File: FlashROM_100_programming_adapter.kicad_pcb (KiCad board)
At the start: 2 copper layers, 16.8 x 34.5 mm, 3 parts, among them J1 LH535618 Socket, U1 28C256 pinout to programmer

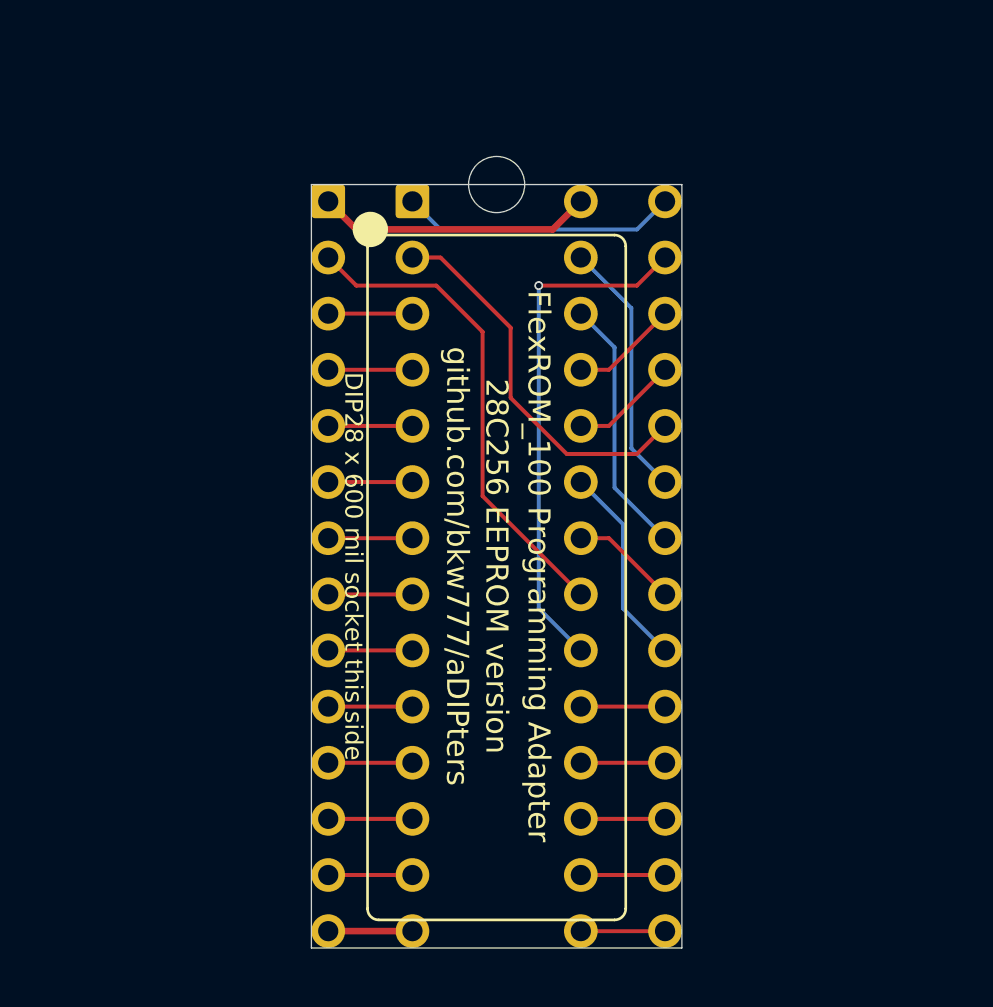
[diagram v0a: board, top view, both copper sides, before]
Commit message: Add FlashROM_100. /WE pin on FlexROM_100
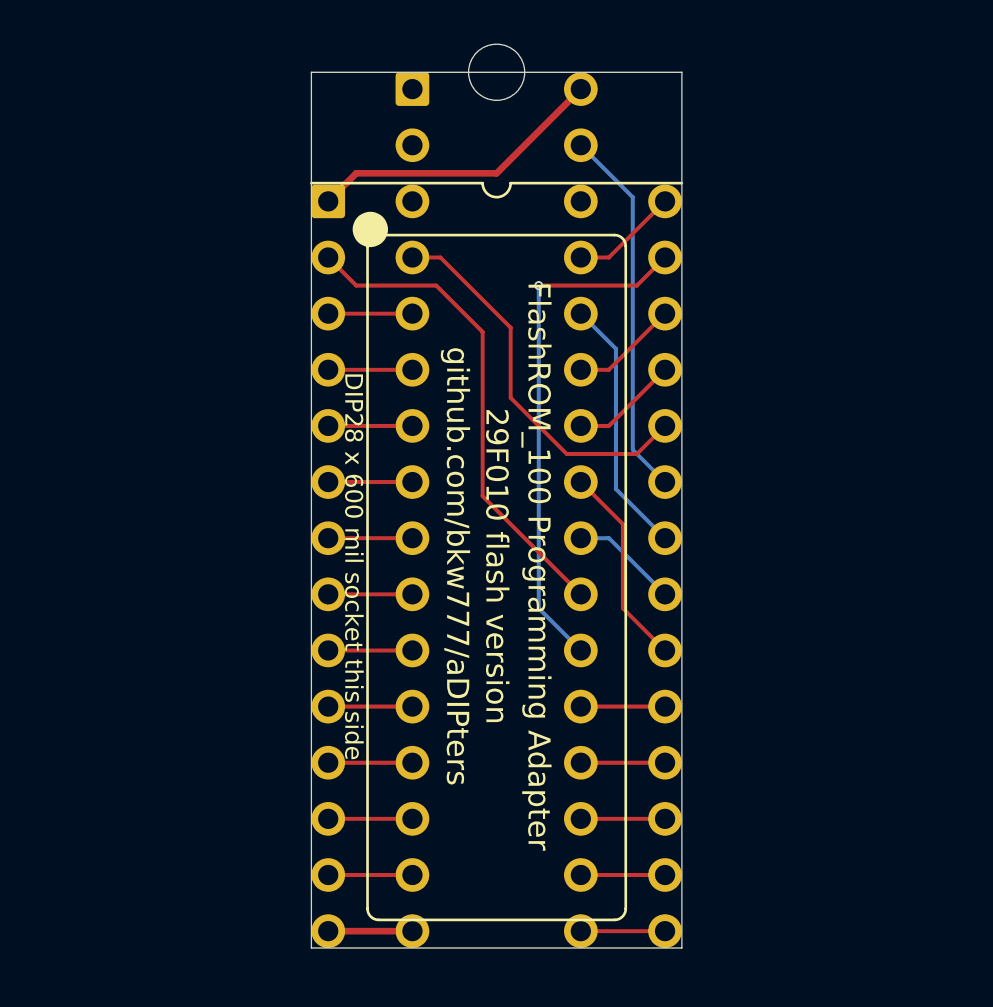
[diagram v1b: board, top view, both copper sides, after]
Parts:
- U1: value 28C256 pinout to programmer -> 29F010 pins to programmer; footprint 000_LOCAL:2x28_0.3_0.1_pins -> 000_LOCAL:DIP32_0.3
- moved polarity notch 5.08 mm to (150.0, 77.6)
- moved U1 2.54 mm to (150.0, 97.5)
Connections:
- U1 pad 1: /A14 -> (no net)
- U1 pad 10: /A0 -> /A2
- U1 pad 11: /D0 -> /A1
- U1 pad 12: /D1 -> /A0
- U1 pad 13: /D2 -> /D0
- U1 pad 14: /GND -> /D1
- U1 pad 15: /D3 -> /D2
- U1 pad 16: /D4 -> /GND
- U1 pad 17: /D5 -> /D3
- U1 pad 18: /D6 -> /D4
- U1 pad 19: /D7 -> /D5
- U1 pad 2: /A12 -> (no net)
- U1 pad 20: /~CE -> /D6
- U1 pad 21: /A10 -> /D7
- U1 pad 22: /~OE -> /~CE
- U1 pad 23: /A11 -> /A10
- U1 pad 24: /A9 -> /~OE
- U1 pad 25: /A8 -> /A11
- U1 pad 26: /A13 -> /A9
- U1 pad 27: /~WE -> /A8
- U1 pad 28: /VCC -> /A13
- U1 pad 3: /A7 -> (no net)
- U1 pad 4: /A6 -> /A12
- U1 pad 5: /A5 -> /A7
- U1 pad 6: /A4 -> /A6
- U1 pad 7: /A3 -> /A5
- U1 pad 8: /A2 -> /A4
- U1 pad 9: /A1 -> /A3
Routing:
- net /A14: track 12.5 -> 4.86 mm
- net /~WE: track 11.7 -> 16.8 mm
- net /VCC: track 12.5 -> 13.5 mm
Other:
- board size 16.8 x 34.5 mm -> 16.8 x 39.6 mm
- board text added: "29F010 flash version"
- board text added: "FlashROM_100 Programming Adapter"
- board text removed: "28C256 EEPROM version"
- board text removed: "FlexROM_100 Programming Adapter"
- board text removed: "tandy.wiki/FlexROM_100"

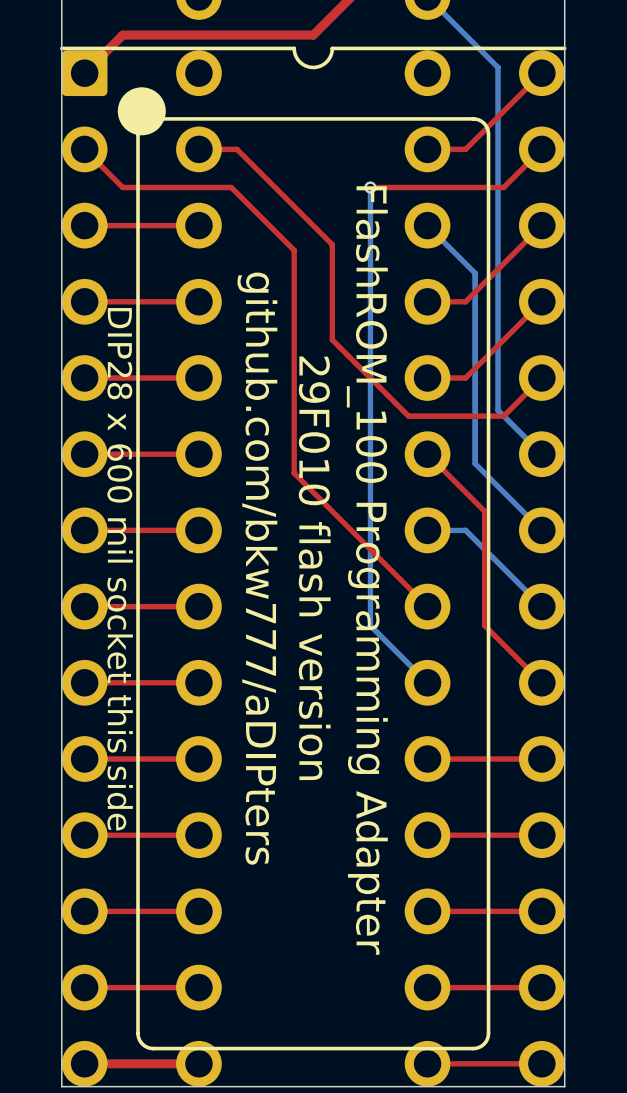
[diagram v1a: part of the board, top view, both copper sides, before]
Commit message: add FlashROM_100_tsop
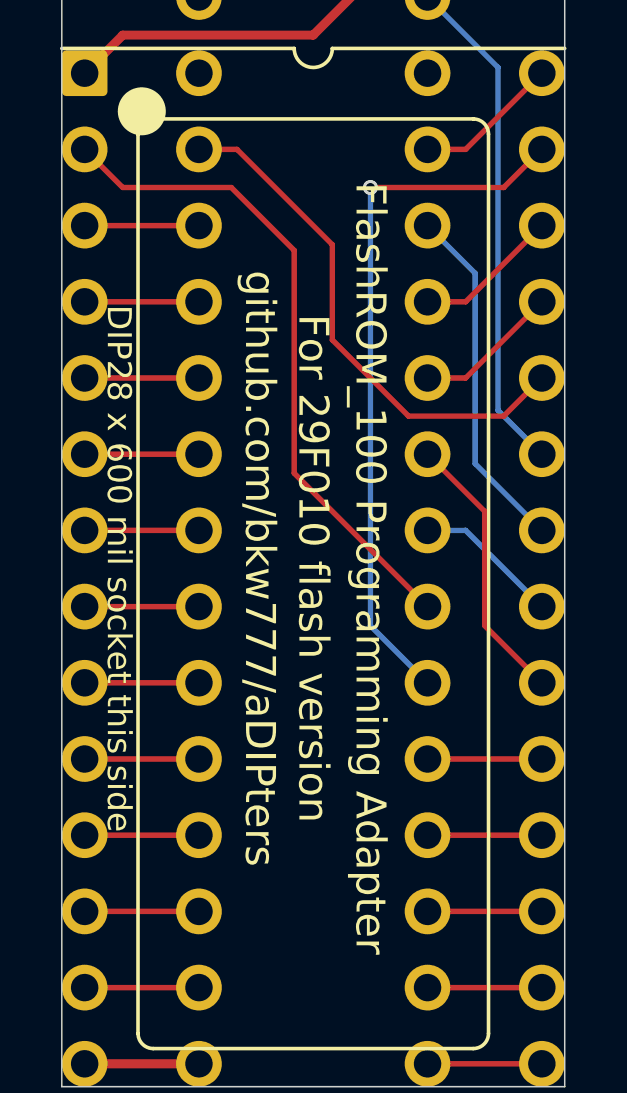
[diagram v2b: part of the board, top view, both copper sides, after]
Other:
- net class Default: via_dia 0.4 -> 0.5; via_drill 0.25 -> 0.3
- rule via_min_drill: 0.25 -> 0.3
- rule via_min_size: 0.4 -> 0.5
- board text added: "For 29F010 flash version"
- board text removed: "29F010 flash version"
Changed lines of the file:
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@@
-(kicad_pcb (version 20171130) (host pcbnew 5.1.7-a382d34a8~87~ubuntu20.04.1)
+(kicad_pcb (version 20171130) (host pcbnew 5.1.9-73d0e3b20d~88~ubuntu20.10.1)
   (general
     (thickness 1.6)
@@
     (nets 29)
   )
-  (page A4)
+  (page USLetter)
+  (title_block
+    (title "Programming Adapter for FlashROM_100")
+    (date 2021-03-07)
+    (rev 002)
+    (company "Brian K. White - b.kenyon.w@gmail.com")
+  )
   (layers
     (0 F.Cu signal)
@@
     (zone_45_only no)
     (trace_min 0.16)
-    (via_size 0.4)
-    (via_drill 0.25)
-    (via_min_size 0.4)
-    (via_min_drill 0.25)
-    (uvia_size 0.4)
-    (uvia_drill 0.25)
+    (via_size 0.5)
+    (via_drill 0.3)
+    (via_min_size 0.5)
+    (via_min_drill 0.3)
+    (uvia_size 0.5)
+    (uvia_drill 0.3)
     (uvias_allowed no)
-    (uvia_min_size 0.4)
-    (uvia_min_drill 0.25)
+    (uvia_min_size 0.5)
+    (uvia_min_drill 0.3)
     (edge_width 0.05)
     (segment_width 0.2)
@@
     (pad_drill 0.9144)
     (pad_to_mask_clearance 0)
+    (solder_mask_min_width 0.22)
     (aux_axis_origin 0 0)
     (grid_origin 150 100)
@@
       (outputformat 1)
       (mirror false)
-      (drillshape 1)
+      (drillshape 0)
       (scaleselection 1)
-      (outputdirectory ""))
+      (outputdirectory "GERBER_FlashROM_100_programming_adapter"))
   )
   (net 0 "")
@@
     (clearance 0.16)
     (trace_width 0.18)
-    (via_dia 0.4)
-    (via_drill 0.25)
-    (uvia_dia 0.4)
-    (uvia_drill 0.25)
+    (via_dia 0.5)
+    (via_drill 0.3)
+    (uvia_dia 0.5)
+    (uvia_drill 0.3)
     (add_net /A0)
     (add_net /A1)
@@
       (effects (font (size 1 1) (thickness 0.15)))
     )
+    (fp_line (start -8.382 -17.272) (end -8.382 17.272) (layer F.CrtYd) (width 0.01))
+    (fp_line (start -8.382 17.272) (end 8.382 17.272) (layer F.CrtYd) (width 0.01))
+    (fp_line (start 8.382 17.272) (end 8.382 -17.272) (layer F.CrtYd) (width 0.01))
     (fp_line (start 8.382 -17.272) (end -8.382 -17.272) (layer F.CrtYd) (width 0.01))
-    (fp_line (start 8.382 17.272) (end 8.382 -17.272) (layer F.CrtYd) (width 0.01))
-    (fp_line (start -8.382 17.272) (end 8.382 17.272) (layer F.CrtYd) (width 0.01))
-    (fp_line (start -8.382 -17.272) (end -8.382 17.272) (layer F.CrtYd) (width 0.01))
     (fp_text user %R (at 0.27 3.12) (layer F.Fab)
       (effects (font (size 1 1) (thickness 0.15)))
@@
   (gr_arc (start 150 82.6645) (end 149.365 82.6645) (angle -180) (layer F.SilkS) (width 0.12))
   (gr_line (start 141.618 82.6645) (end 149.365 82.6645) (layer F.SilkS) (width 0.12))
-  (gr_text "29F010 flash version" (at 150 100 -90) (layer F.SilkS)
+  (gr_text "For 29F010 flash version" (at 150 100 -90) (layer F.SilkS)
     (effects (font (size 1 1) (thickness 0.15)))
   )
@@
   (segment (start 157.62 96.19) (end 156.1595 94.7295) (width 0.18) (layer B.Cu) (net 27))
   (segment (start 151.905 87.3) (end 151.905 87.3) (width 0.18) (layer F.Cu) (net 28))
-  (via (at 151.905 87.3) (size 0.4) (drill 0.25) (layers F.Cu B.Cu) (net 28))
+  (via (at 151.905 87.3) (size 0.5) (drill 0.3) (layers F.Cu B.Cu) (net 28) (status 1000000))
   (segment (start 151.905 101.905) (end 153.81 103.81) (width 0.18) (layer B.Cu) (net 28))
   (segment (start 151.905 87.3) (end 151.905 101.905) (width 0.18) (layer B.Cu) (net 28))

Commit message: kicad 6
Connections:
- net /~CE renamed /~{CE}
- net /~OE renamed /~{OE}
- net /~WE renamed /~{WE}
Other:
- net class Default removed

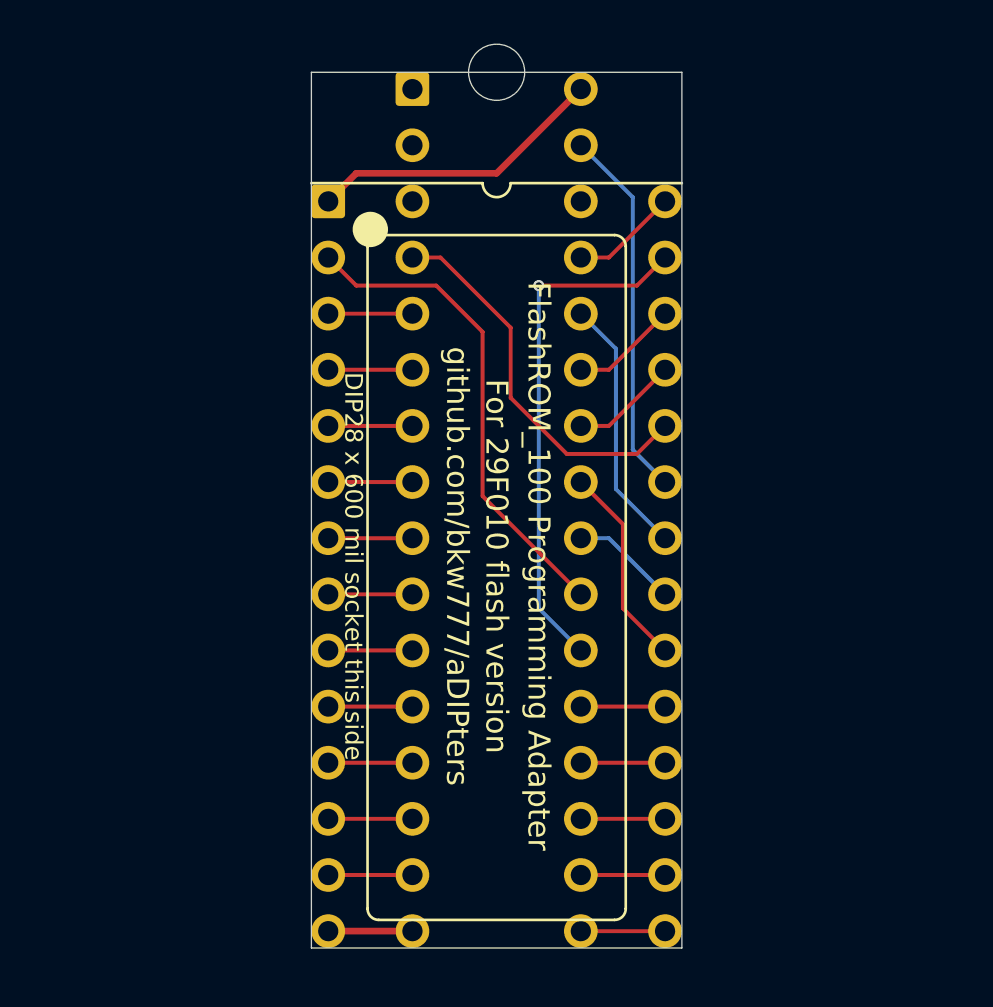
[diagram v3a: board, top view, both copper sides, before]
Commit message: Fix wrong pinout on FlashROM_100 TSOPgit add -A!
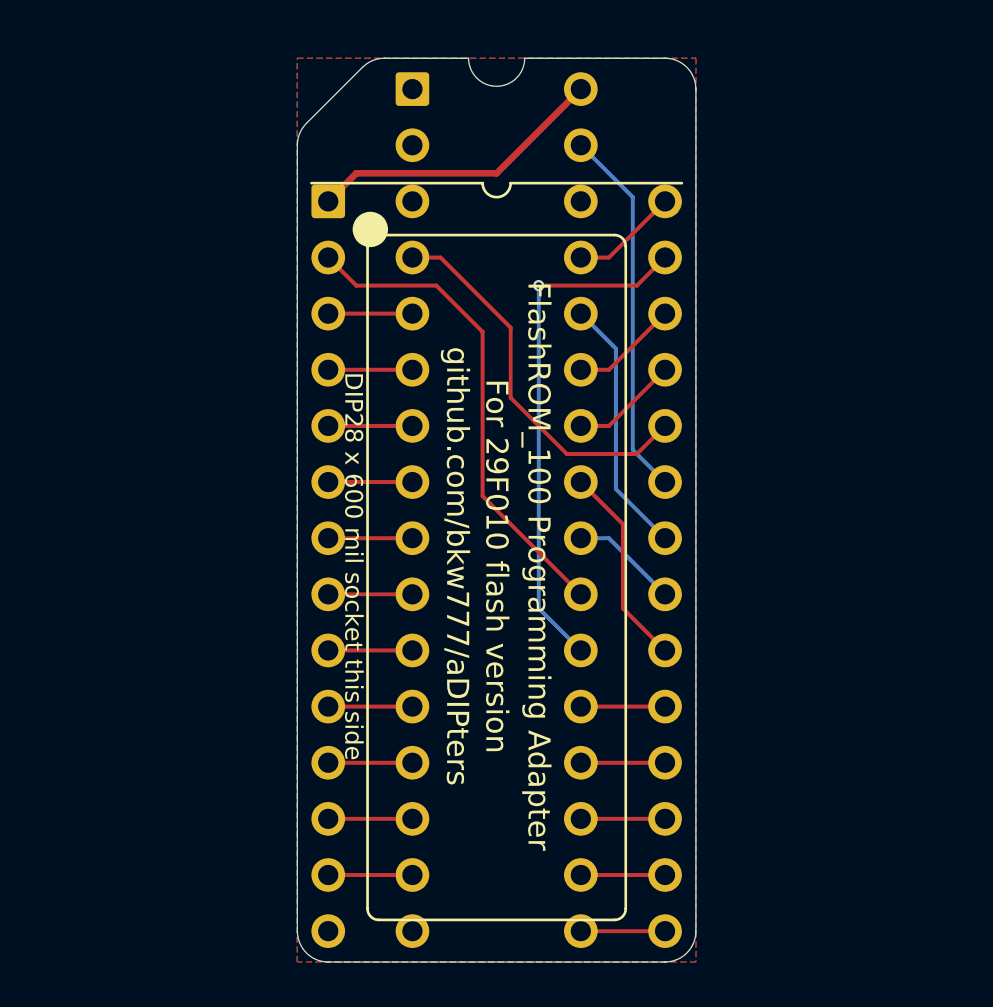
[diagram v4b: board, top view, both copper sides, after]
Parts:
- removed polarity notch: NPTH_0.1, 000_LOCAL:NPTH_0.1
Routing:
- net /GND: track 3.81 -> 0.00 mm
- added copper zone on B.Cu, net /GND
- added copper zone on F.Cu, net /GND
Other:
- board size 16.8 x 39.6 mm -> 18 x 40.9 mm
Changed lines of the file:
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@@
   (title_block
     (title "Programming Adapter for FlashROM_100")
-    (date "2021-03-07")
-    (rev "002")
+    (date "2022-10-11")
+    (rev "003")
     (company "Brian K. White - b.kenyon.w@gmail.com")
   )
@@
     )
   )
-  (footprint "000_LOCAL:NPTH_0.1" (layer "F.Cu")
-    (at 150 77.648)
-    (attr through_hole)
-    (fp_text reference "polarity notch" (at 0 2.54) (layer "F.SilkS") hide
-      (effects (font (size 1.27 1.27) (thickness 0.127)))
-    )
-    (fp_text value "NPTH_0.1" (at 0 -2.54) (layer "F.Fab")
-      (effects (font (size 1.27 1.27) (thickness 0.0127)))
-    )
-    (pad "" np_thru_hole circle locked (at 0 0) (size 2.54 2.54) (drill 2.54) (layers *.Cu *.Mask))
-  )
   (gr_line (start 152.54 77.7115) (end 155.08 77.7115) (layer "B.SilkS") (width 0.12))
   (gr_line (start 144.92 77.7115) (end 147.46 77.7115) (layer "B.SilkS") (width 0.12))
@@
   (gr_arc (start 150.635 82.6645) (mid 150 83.2995) (end 149.365 82.6645) (layer "F.SilkS") (width 0.12))
   (gr_arc (start 155.842 115.494) (mid 155.69321 115.85321) (end 155.334 116.002) (layer "F.SilkS") (width 0.12))
-  (gr_line (start 158.382 77.648) (end 158.382 117.272) (layer "Edge.Cuts") (width 0.05))
-  (gr_line (start 141.618 117.272) (end 141.618 77.648) (layer "Edge.Cuts") (width 0.05))
-  (gr_line (start 141.618 77.648) (end 158.382 77.648) (layer "Edge.Cuts") (width 0.05))
-  (gr_line (start 141.618 117.272) (end 158.382 117.272) (layer "Edge.Cuts") (width 0.05))
+  (gr_line (start 143.932172 77.422172) (end 141.392172 79.962172) (layer "Edge.Cuts") (width 0.05))
+  (gr_arc (start 142.38 117.907) (mid 141.392172 117.497828) (end 140.983 116.51) (layer "Edge.Cuts") (width 0.05))
+  (gr_line (start 140.983 116.51) (end 140.983 80.95) (layer "Edge.Cuts") (width 0.05))
+  (gr_arc (start 151.27 77.013) (mid 150 78.283) (end 148.73 77.013) (layer "Edge.Cuts") (width 0.05))
+  (gr_arc (start 157.62 77.013) (mid 158.607828 77.422172) (end 159.017 78.41) (layer "Edge.Cuts") (width 0.05))
+  (gr_arc (start 140.983 80.95) (mid 141.08934 80.415391) (end 141.392172 79.962172) (layer "Edge.Cuts") (width 0.05))
+  (gr_line (start 142.38 117.907) (end 157.62 117.907) (layer "Edge.Cuts") (width 0.05))
+  (gr_arc (start 159.017 116.51) (mid 158.607828 117.497828) (end 157.62 117.907) (layer "Edge.Cuts") (width 0.05))
+  (gr_arc (start 143.932172 77.422172) (mid 144.385391 77.119341) (end 144.92 77.013) (layer "Edge.Cuts") (width 0.05))
+  (gr_line (start 151.27 77.013) (end 157.62 77.013) (layer "Edge.Cuts") (width 0.05))
+  (gr_line (start 144.92 77.013) (end 148.73 77.013) (layer "Edge.Cuts") (width 0.05))
+  (gr_line (start 159.017 116.51) (end 159.017 78.41) (layer "Edge.Cuts") (width 0.05))
   (gr_text "Two middle rows, pins to programmer this side" (at 148.1585 100 90) (layer "B.SilkS")
     (effects (font (size 0.8 0.8) (thickness 0.1)) (justify mirror))
@@
   (segment (start 155.08 91.11) (end 157.62 88.57) (width 0.18) (layer "F.Cu") (net 23))
   (segment (start 142.38 113.97) (end 146.19 113.97) (width 0.18) (layer "F.Cu") (net 24))
-  (segment (start 142.38 116.51) (end 146.19 116.51) (width 0.3) (layer "F.Cu") (net 25))
   (segment (start 155.08 86.03) (end 153.81 86.03) (width 0.18) (layer "F.Cu") (net 26))
   (segment (start 157.62 83.49) (end 155.08 86.03) (width 0.18) (layer "F.Cu") (net 26))
@@
   (segment (start 151.905 87.3) (end 151.905 101.905) (width 0.18) (layer "B.Cu") (net 28))
   (segment (start 151.905 101.905) (end 153.81 103.81) (width 0.18) (layer "B.Cu") (net 28))
+  (zone (net 25) (net_name "/GND") (layer "F.Cu") (hatch edge 0.508)
+    (connect_pads yes (clearance 0.2))
+    (min_thickness 0.2) (filled_areas_thickness no)
+    (fill yes (thermal_gap 0.508) (thermal_bridge_width 0.508))
+    (polygon
+      (pts
+        (xy 159.017 117.907)
+        (xy 140.983 117.907)
+        (xy 140.983 77.013)
+        (xy 159.017 77.013)
+      )
+    )
+  )
+  (zone (net 25) (net_name "/GND") (layer "B.Cu") (hatch edge 0.508)
+    (connect_pads yes (clearance 0.2))
+    (min_thickness 0.2) (filled_areas_thickness no)
+    (fill yes (thermal_gap 0.508) (thermal_bridge_width 0.508))
+    (polygon
+      (pts
+        (xy 159.017 117.907)
+        (xy 140.983 117.907)
+        (xy 140.983 77.013)
+        (xy 159.017 77.013)
+      )
+    )
+  )
 )

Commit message: various minor cleanups
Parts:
- moved U1 2.54 mm to (150.0, 100.0), turned to 90 degrees
- moved J1 2.54 mm to (152.5, 100.0), turned to 90 degrees
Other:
- board size 18 x 40.9 mm -> 40.9 x 18 mm
